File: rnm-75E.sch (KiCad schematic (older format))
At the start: 217 parts, among them J1 AVR-ISP-6, J2 USB_C_Receptacle_USB2.0, J3 Conn_01x04, SW1 SW_Push, SW2 Rotary_Encoder_Switch, U1 AT90USB646-AU, Y1 Crystal_GND24_Small

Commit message: added ground fill
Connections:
- net LED_PIN: now also U1.10 (PB0); no longer U1.9 (PE3)
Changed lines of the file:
@@
 Text GLabel 5350 8900 2    50   Input ~ 0
 SDA
-Text GLabel 3300 9000 0    50   Input ~ 0
+Text GLabel 4500 7800 2    50   Input ~ 0
 LED_PIN
 Text GLabel 3300 9600 0    50   Input ~ 0

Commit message: gerbers
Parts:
- added R2: 1k, Resistor_SMD:R_0805_2012Metric, symbol Device:R_Small
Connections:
- net GND: now also SW2.C
- net LED: now also R2.2; no longer D95.4 (DIN)
- new net: D95.4 (DIN), R2.1
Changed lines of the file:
@@
 Text GLabel 4500 9400 2    50   Input ~ 0
 LED
-Text GLabel 9600 2850 0    50   Input ~ 0
+Text GLabel 9150 2850 0    50   Input ~ 0
 LED
 Wire Wire Line
@@
 Connection ~ 14050 3150
 Connection ~ 12900 3150
+$Comp
+L Device:R_Small R2
+U 1 1 61A60D7F
+P 9250 2850
+F 0 "R2" V 9054 2850 50  0000 C CNN
+F 1 "1k" V 9145 2850 50  0000 C CNN
+F 2 "Resistor_SMD:R_0805_2012Metric" H 9250 2850 50  0001 C CNN
+F 3 "~" H 9250 2850 50  0001 C CNN
+	1    9250 2850
+	0    1    1    0
+$EndComp
+Wire Wire Line
+	9350 2850 9600 2850
+$Comp
+L power:GND #PWR?
+U 1 1 61C02F04
+P 11750 4750
+F 0 "#PWR?" H 11750 4500 50  0001 C CNN
+F 1 "GND" H 11755 4577 50  0000 C CNN
+F 2 "" H 11750 4750 50  0001 C CNN
+F 3 "" H 11750 4750 50  0001 C CNN
+	1    11750 4750
+	-1   0    0    1
+$EndComp
 $EndSCHEMATC

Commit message: update led resistor
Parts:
- R2: value 1k -> 500
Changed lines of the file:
@@
 P 9250 2850
 F 0 "R2" V 9054 2850 50  0000 C CNN
-F 1 "1k" V 9145 2850 50  0000 C CNN
+F 1 "500" V 9145 2850 50  0000 C CNN
 F 2 "Resistor_SMD:R_0805_2012Metric" H 9250 2850 50  0001 C CNN
 F 3 "~" H 9250 2850 50  0001 C CNN
@@
 	9350 2850 9600 2850
 $Comp
-L power:GND #PWR?
+L power:GND #PWR0119
 U 1 1 61C02F04
 P 11750 4750
-F 0 "#PWR?" H 11750 4500 50  0001 C CNN
+F 0 "#PWR0119" H 11750 4500 50  0001 C CNN
 F 1 "GND" H 11755 4577 50  0000 C CNN
 F 2 "" H 11750 4750 50  0001 C CNN

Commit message: bom + new gerber
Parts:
- J2: footprint Connector_USB:USB_C_Receptacle_HRO_TYPE-C-31-M-12 -> Connector_USB:USB_C_Receptacle_Palconn_UTC16-G
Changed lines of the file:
@@
 F 0 "J2" H 2057 5867 50  0000 C CNN
 F 1 "USB_C_Receptacle_USB2.0" H 2057 5776 50  0000 C CNN
-F 2 "Connector_USB:USB_C_Receptacle_HRO_TYPE-C-31-M-12" H 2100 5000 50  0001 C CNN
+F 2 "Connector_USB:USB_C_Receptacle_Palconn_UTC16-G" H 2100 5000 50  0001 C CNN
 F 3 "https://www.usb.org/sites/default/files/documents/usb_type-c.zip" H 2100 5000 50  0001 C CNN
 	1    1950 5000

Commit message: More stable design
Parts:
- J1: footprint Connector_PinSocket_1.00mm:PinSocket_2x03_P1.00mm_Vertical_SMD -> random_keyboard_parts:Reset_Pretty-Mask
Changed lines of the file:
@@
 F 0 "J1" H 1521 7346 50  0000 R CNN
 F 1 "AVR-ISP-6" H 1521 7255 50  0000 R CNN
-F 2 "Connector_PinSocket_1.00mm:PinSocket_2x03_P1.00mm_Vertical_SMD" V 1600 7300 50  0001 C CNN
+F 2 "random_keyboard_parts:Reset_Pretty-Mask" V 1600 7300 50  0001 C CNN
 F 3 " ~" H 575 6700 50  0001 C CNN
 	1    1850 7250

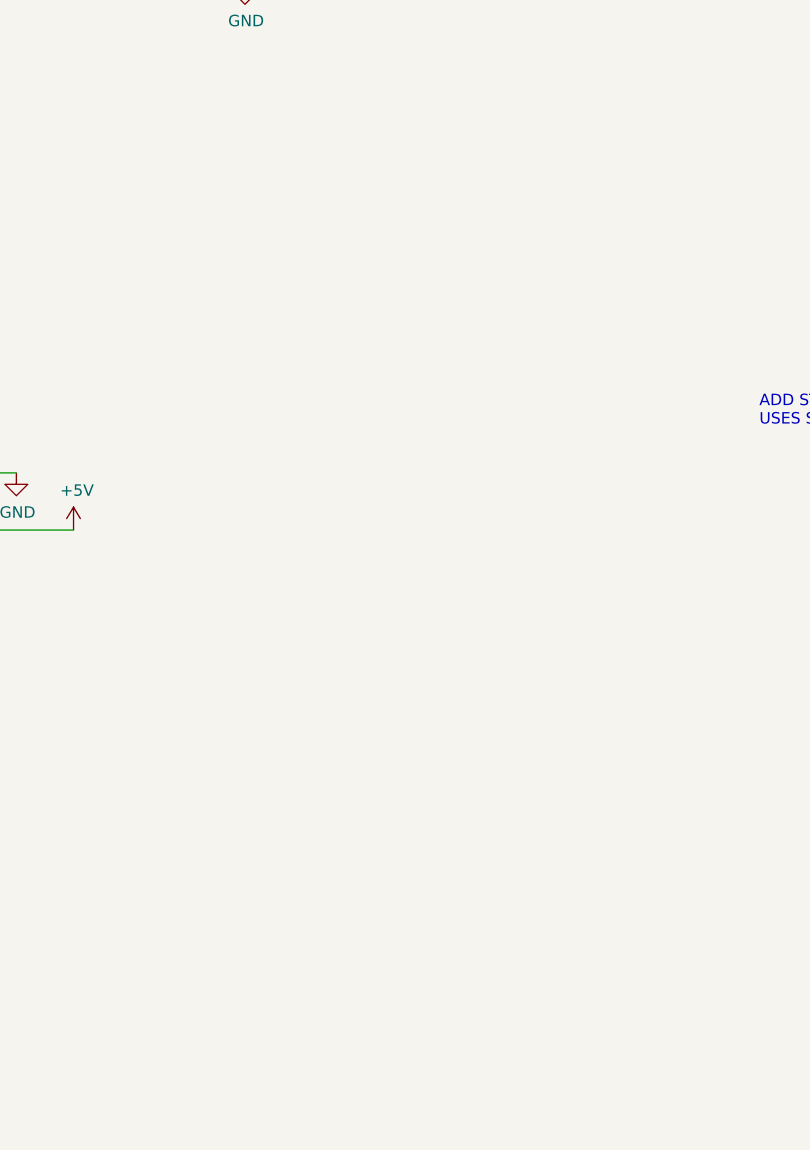
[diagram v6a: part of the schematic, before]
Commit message: added new mcu
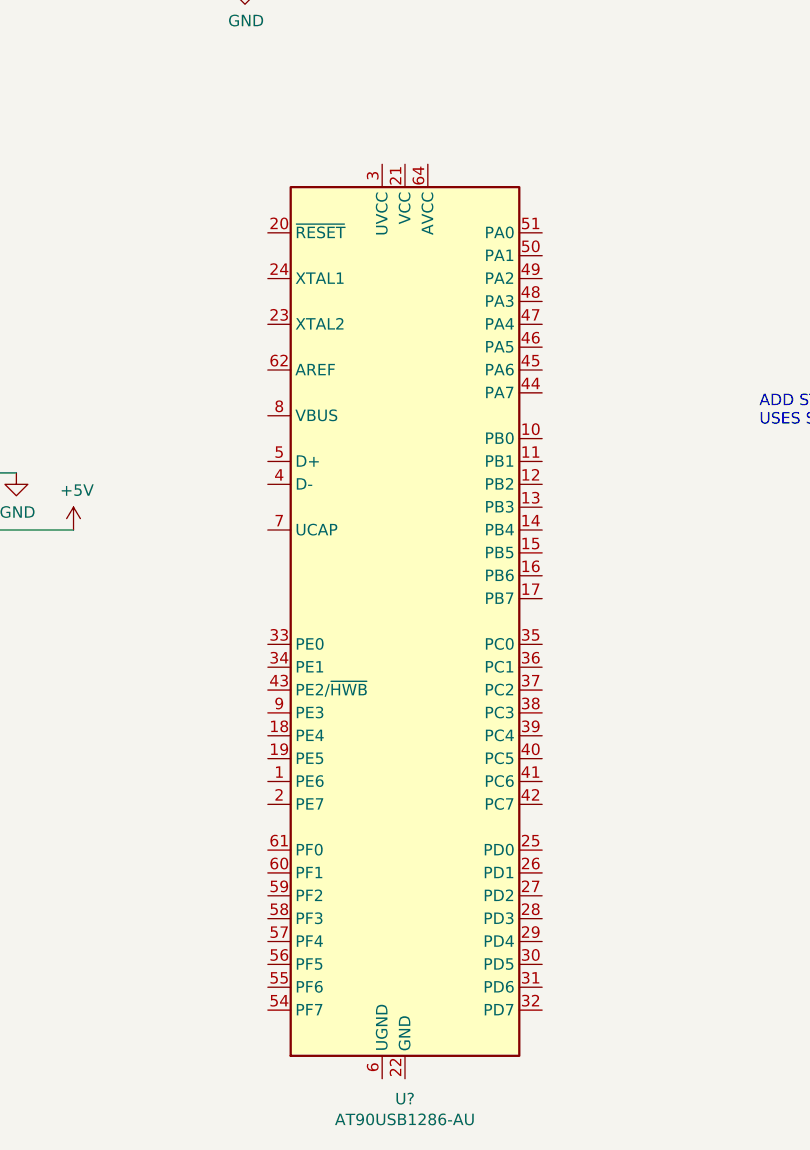
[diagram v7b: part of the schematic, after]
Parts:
- added U?: AT90USB1286-AU, Package_QFP:TQFP-64_14x14mm_P0.8mm, symbol MCU_Microchip_AVR:AT90USB1286-AU
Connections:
- new net: U?.21 (VCC), U?.52 (VCC)
- new net: U?.22 (GND), U?.53 (GND), U?.63 (GND)
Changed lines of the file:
@@
+	1    0    0    -1
+$EndComp
+$Comp
+L MCU_Microchip_AVR:AT90USB1286-AU U?
+U 1 1 61F70342
+P 7750 9100
+F 0 "U?" H 7750 7011 50  0000 C CNN
+F 1 "AT90USB1286-AU" H 7750 6920 50  0000 C CNN
+F 2 "Package_QFP:TQFP-64_14x14mm_P0.8mm" H 7750 9100 50  0001 C CIN
+F 3 "http://ww1.microchip.com/downloads/en/DeviceDoc/doc7593.pdf" H 7750 9100 50  0001 C CNN
+	1    7750 9100
 	1    0    0    -1
 $EndComp

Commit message: srv05 added
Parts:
- removed ESD1: PRTR5V0U2X, Package_TO_SOT_SMD:SOT-143, symbol Power_Protection:PRTR5V0U2X
- removed U1: AT90USB646-AU, Package_QFP:TQFP-64_14x14mm_P0.8mm, symbol MCU_Microchip_AVR:AT90USB646-AU
- added U2: SRV05-4, Package_TO_SOT_SMD:SOT-23-6, symbol Power_Protection:SRV05-4
- gave numbers to parts that had none: 1
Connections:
- net +5V: now also U1.21 (VCC), U1.3 (UVCC), U1.52 (VCC), U1.64 (AVCC), U1.8 (VBUS), U2.5 (VP)
- net COL0: now also U1.44 (PA7)
- net COL1: now also U1.45 (PA6)
- net COL10: now also U1.19 (PE5)
- net COL11: now also U1.27 (PD2)
- net COL12: now also U1.28 (PD3)
- net COL13: now also U1.29 (PD4)
- net COL14: now also U1.30 (PD5)
- net COL15: now also U1.31 (PD6)
- net COL2: now also U1.46 (PA5)
- net COL3: now also U1.47 (PA4)
- net COL4: now also U1.48 (PA3)
- net COL5: now also U1.49 (PA2)
- net COL6: now also U1.50 (PA1)
- net COL7: now also U1.51 (PA0)
- net COL8: now also U1.17 (PB7)
- net COL9: now also U1.18 (PE4)
- net D+: now also U1.5 (D+), U2.3 (IO2)
- net D-: now also U1.4 (D-), U2.1 (IO1)
- net ENCODER+: now also U1.55 (PF6)
- net ENCODER-: now also U1.54 (PF7)
- net GND: now also U1.22 (GND), U1.53 (GND), U1.6 (UGND), U1.63 (GND), U2.2 (VN)
- net LED: now also U1.42 (PC7)
- net LED_PIN: now also U1.33 (PE0)
- net MISO: now also U1.13 (PB3)
- net MOSI: now also U1.12 (PB2)
- net RESET: now also U1.20 (~RESET)
- net ROWA: now also U1.60 (PF1)
- net ROWB: now also U1.59 (PF2)
- net ROWC: now also U1.58 (PF3)
- net ROWD: now also U1.57 (PF4)
- net ROWE: now also U1.56 (PF5)
- net ROWF: now also U1.61 (PF0)
- net SCK: now also U1.11 (PB1)
- net SCL: now also U1.25 (PD0)
- net SDA: now also U1.26 (PD1)
- net XTAL1: now also U1.24 (XTAL1)
- net XTAL2: now also U1.23 (XTAL2)
- net at C_ucap1.2: now also U1.7 (UCAP)
- net at R_SW2.1: now also U1.43 (PE2/~HWB)
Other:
- moved on the sheet: U1
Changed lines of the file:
@@
 $EndComp
 $Comp
-L Power_Protection:PRTR5V0U2X ESD1
-U 1 1 609E72F8
-P 4850 5050
-F 0 "ESD1" H 5300 4800 50  0000 L CNN
-F 1 "PRTR5V0U2X" H 5300 4700 50  0000 L CNN
-F 2 "Package_TO_SOT_SMD:SOT-143" H 4910 5050 50  0001 C CNN
-F 3 "https://assets.nexperia.com/documents/data-sheet/PRTR5V0U2X.pdf" H 4910 5050 50  0001 C CNN
-	1    4850 5050
-	1    0    0    -1
-$EndComp
-$Comp
 L power:+5V #PWR0107
 U 1 1 609E94CA
-P 4850 4550
-F 0 "#PWR0107" H 4850 4400 50  0001 C CNN
-F 1 "+5V" H 4865 4723 50  0000 C CNN
-F 2 "" H 4850 4550 50  0001 C CNN
-F 3 "" H 4850 4550 50  0001 C CNN
-	1    4850 4550
+P 4850 4200
+F 0 "#PWR0107" H 4850 4050 50  0001 C CNN
+F 1 "+5V" H 4865 4373 50  0000 C CNN
+F 2 "" H 4850 4200 50  0001 C CNN
+F 3 "" H 4850 4200 50  0001 C CNN
+	1    4850 4200
 	1    0    0    -1
 $EndComp
@@
 L power:GND #PWR0108
 U 1 1 609EA217
-P 4850 5550
-F 0 "#PWR0108" H 4850 5300 50  0001 C CNN
-F 1 "GND" H 4855 5377 50  0000 C CNN
-F 2 "" H 4850 5550 50  0001 C CNN
-F 3 "" H 4850 5550 50  0001 C CNN
-	1    4850 5550
+P 4850 5650
+F 0 "#PWR0108" H 4850 5400 50  0001 C CNN
+F 1 "GND" H 4855 5477 50  0000 C CNN
+F 2 "" H 4850 5650 50  0001 C CNN
+F 3 "" H 4850 5650 50  0001 C CNN
+	1    4850 5650
 	1    0    0    -1
 $EndComp
-Text GLabel 5350 5050 2    50   Input ~ 0
+Text GLabel 4350 5250 0    50   Input ~ 0
 D+
 Text GLabel 4350 5050 0    50   Input ~ 0
@@
 Text GLabel 5350 8900 2    50   Input ~ 0
 SDA
-Text GLabel 4500 7800 2    50   Input ~ 0
+Text GLabel 3300 8700 0    50   Input ~ 0
 LED_PIN
 Text GLabel 3300 9600 0    50   Input ~ 0
@@
 $EndComp
 $Comp
-L MCU_Microchip_AVR:AT90USB646-AU U1
-U 1 1 61783827
+L MCU_Microchip_AVR:AT90USB1286-AU U1
+U 1 1 61F70342
 P 3900 8600
-F 0 "U1" H 4300 6600 50  0000 C CNN
-F 1 "AT90USB646-AU" H 4350 6500 50  0000 C CNN
+F 0 "U1" H 3900 6511 50  0000 C CNN
+F 1 "AT90USB1286-AU" H 3900 6420 50  0000 C CNN
 F 2 "Package_QFP:TQFP-64_14x14mm_P0.8mm" H 3900 8600 50  0001 C CIN
 F 3 "http://ww1.microchip.com/downloads/en/DeviceDoc/doc7593.pdf" H 3900 8600 50  0001 C CNN
@@
 $EndComp
 $Comp
-L MCU_Microchip_AVR:AT90USB1286-AU U?
-U 1 1 61F70342
-P 7750 9100
-F 0 "U?" H 7750 7011 50  0000 C CNN
-F 1 "AT90USB1286-AU" H 7750 6920 50  0000 C CNN
-F 2 "Package_QFP:TQFP-64_14x14mm_P0.8mm" H 7750 9100 50  0001 C CIN
-F 3 "http://ww1.microchip.com/downloads/en/DeviceDoc/doc7593.pdf" H 7750 9100 50  0001 C CNN
-	1    7750 9100
+L Power_Protection:SRV05-4 U2
+U 1 1 61F97F7D
+P 4850 5150
+F 0 "U2" H 4850 5831 50  0000 C CNN
+F 1 "SRV05-4" H 4850 5740 50  0000 C CNN
+F 2 "Package_TO_SOT_SMD:SOT-23-6" H 5550 4700 50  0001 C CNN
+F 3 "http://www.onsemi.com/pub/Collateral/SRV05-4-D.PDF" H 4850 5150 50  0001 C CNN
+	1    4850 5150
 	1    0    0    -1
 $EndComp
+Wire Wire Line
+	4850 4650 4850 4200
 $EndSCHEMATC
